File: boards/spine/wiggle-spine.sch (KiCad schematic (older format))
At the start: 0 parts

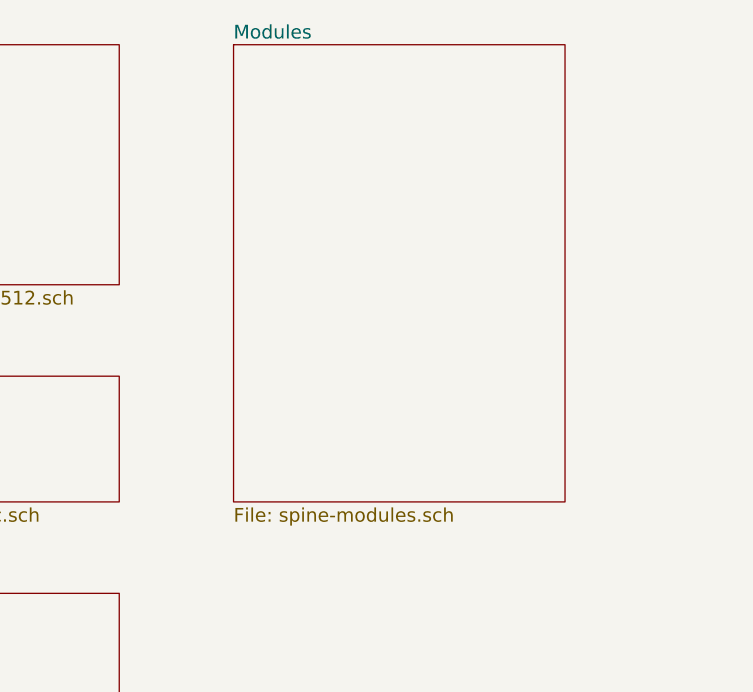
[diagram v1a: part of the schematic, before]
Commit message: Simpler indicator LED strategy
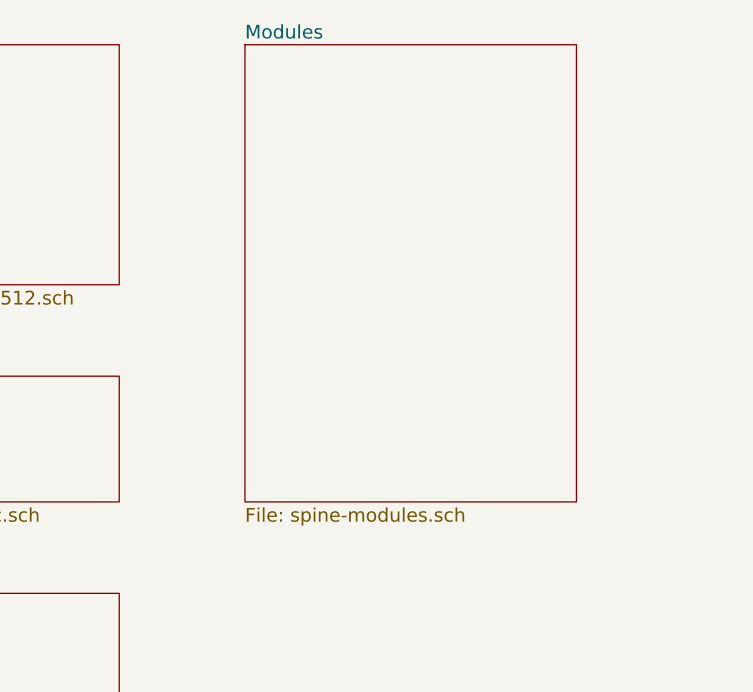
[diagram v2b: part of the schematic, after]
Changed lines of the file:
@@
 $EndSheet
 $Sheet
-S 7850 1600 1450 2000
+S 7900 1600 1450 2000
 U 5641D2D7
 F0 "Modules" 60
@@
 72 0F 1C A9 DC 70 49 CB 79 33 88 85 99 AD 01 6C 4B 10 FC 3B 13 DE 3B 37 68 79 AD 07 BC 00 3C 0E
 3C 31 EE E3 D8 E7 0F 03 D7 7B 9F FB C1 E1 FF 01 18 C4 96 1D B8 0E 40 07 00 00 00 00 49 45 4E 44
-AE 42 60 82 00
+AE 42 60 82 A3
 EndData
 $EndBitmap
